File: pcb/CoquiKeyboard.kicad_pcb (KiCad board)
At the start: 2 copper layers, 307.2 x 79.8 mm, 126 parts, among them SW1 SW_Push, U1 ATmega32U4-AU, Y1 16MHz

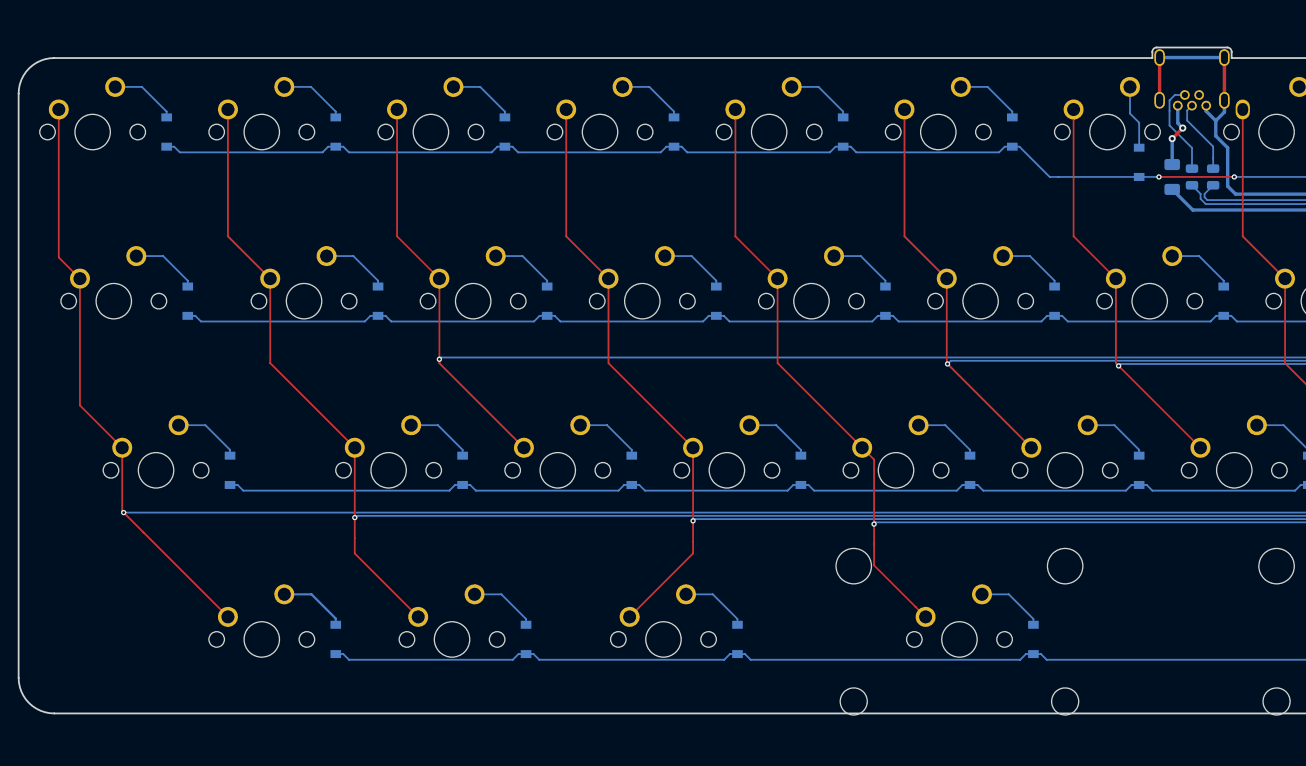
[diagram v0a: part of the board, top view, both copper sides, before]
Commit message: update schematics to use with newer USB-C
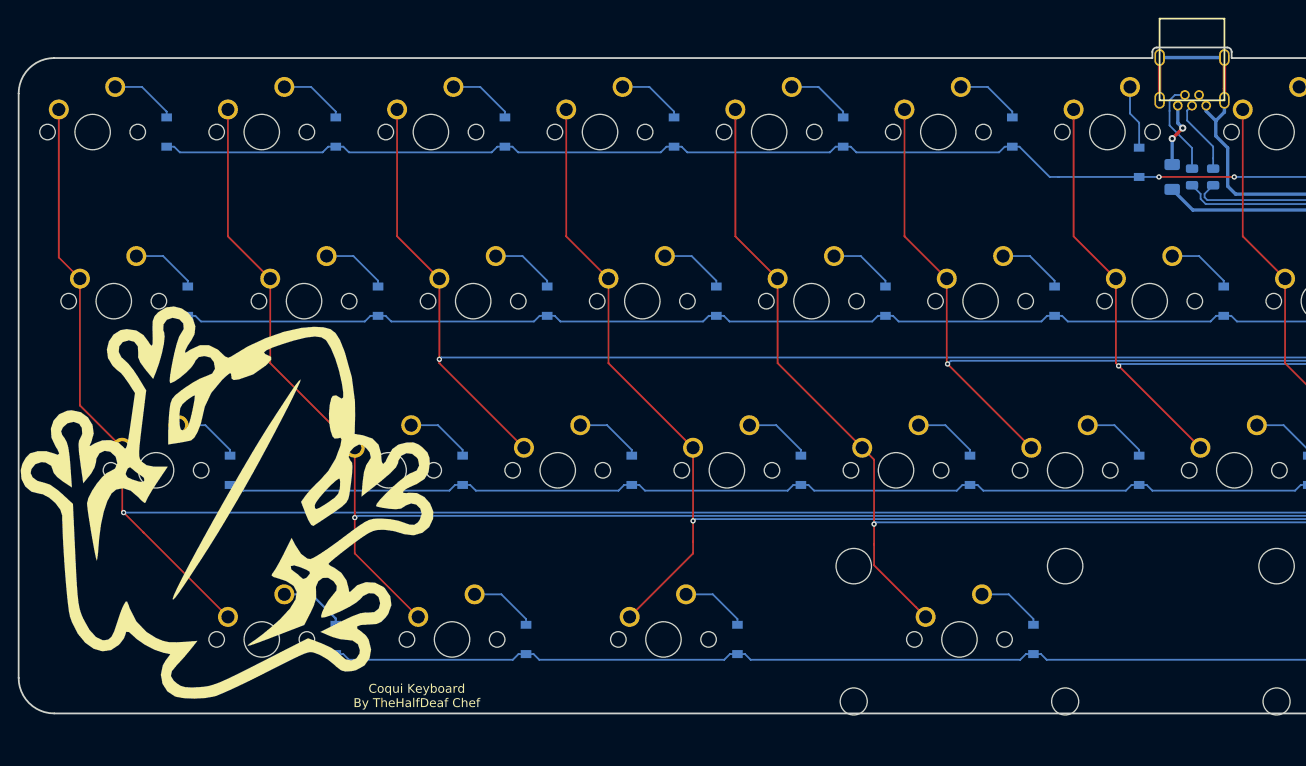
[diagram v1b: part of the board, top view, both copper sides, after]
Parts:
- added G***: LOGO, pcb:CoquiLogo, F.Cu at (44.5, 69.1)
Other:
- board text added: "Coqui Keyboard By TheHalfDeaf Chef"

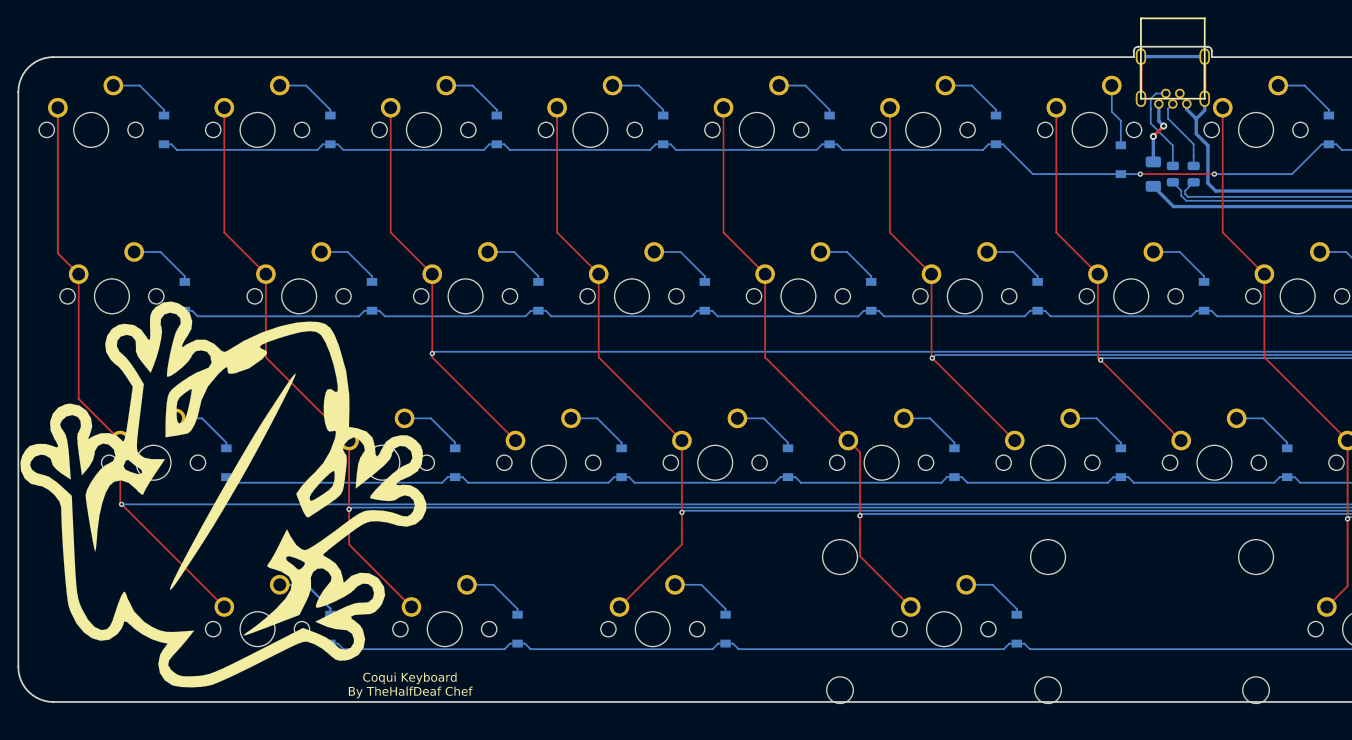
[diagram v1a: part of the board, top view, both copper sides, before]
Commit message: replaced old footprint with new
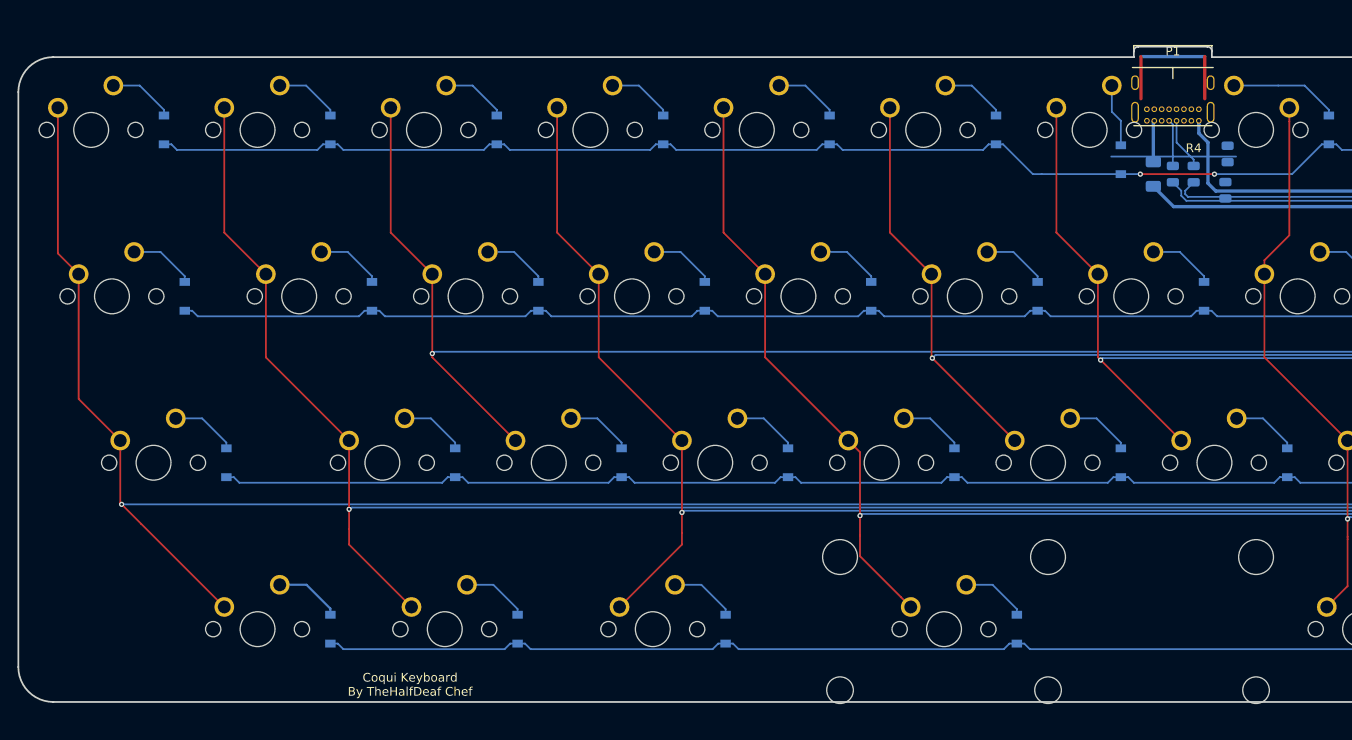
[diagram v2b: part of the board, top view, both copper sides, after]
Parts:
- removed G***: LOGO, pcb:CoquiLogo
- removed USB1: USB Mini, local:USB-Mini-B_ LCSC-C46398
- added P1: USB_C_Plug_USB2.0, Type-C:USB_C_GCT_USB4085, F.Cu at (152.4, 21.4)
- added R1: 5k1, Resistor_SMD:R_0805_2012Metric, B.Cu at (158.4, 35.5)
- added R2: 5k1, Resistor_SMD:R_0805_2012Metric, B.Cu at (158.7, 31.3)
- MX26: renamed from MX8; moved to B.Cu
- turned MX26 to 180 degrees
- renumbered D18 to D10, D32 to D11, D4 to D12, D19 to D13, D33 to D14, D46 to D15, D5 to D16, D20 to D17, D34 to D18, D47 to D19, D16 to D2, D6 to D20, D35 to D22, D7 to D23, D22 to D24, D36 to D25, D8 to D26, D23 to D27, D37 to D28, D48 to D29, D30 to D3, D9 to D30, D24 to D31, D38 to D32, D10 to D33, D25 to D34, D39 to D35, D49 to D36, D11 to D37, D26 to D38, D40 to D39, D44 to D4, D50 to D40, D12 to D41, D27 to D42, D41 to D43, D51 to D44, D13 to D45, D28 to D46, D52 to D47, D14 to D48, D42 to D49, D2 to D5, D53 to D50, D15 to D51, D29 to D52, D43 to D53, D17 to D6, D31 to D7, D45 to D8, D3 to D9, MX18 to MX10, MX32 to MX11, MX4 to MX12, MX19 to MX13, MX33 to MX14, MX46 to MX15, MX5 to MX16, MX20 to MX17, MX34 to MX18, MX47 to MX19, MX16 to MX2, MX6 to MX20, MX35 to MX22, MX7 to MX23, MX22 to MX24, MX36 to MX25, MX23 to MX27, MX37 to MX28, MX48 to MX29, MX30 to MX3, MX9 to MX30, MX24 to MX31, MX38 to MX32, MX10 to MX33, MX25 to MX34, MX39 to MX35, MX49 to MX36, MX11 to MX37, MX26 to MX38, MX40 to MX39, MX44 to MX4, MX50 to MX40, MX12 to MX41, MX27 to MX42, MX41 to MX43, MX51 to MX44, MX13 to MX45, MX28 to MX46, MX52 to MX47, MX14 to MX48, MX42 to MX49, MX2 to MX5, MX53 to MX50, MX15 to MX51, MX29 to MX52, MX43 to MX53, MX17 to MX6, MX31 to MX7, MX45 to MX8, MX3 to MX9, R2 to R4, R1 to R5, R4 to R6
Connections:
- U1 pad 1: Net-(U1-Pad1) -> (no net)
- U1 pad 10: Net-(U1-Pad10) -> (no net)
- U1 pad 11: Net-(U1-Pad11) -> (no net)
- U1 pad 12: Net-(U1-Pad12) -> (no net)
- U1 pad 36: Net-(U1-Pad36) -> (no net)
- U1 pad 42: Net-(U1-Pad42) -> (no net)
- U1 pad 9: Net-(U1-Pad9) -> (no net)
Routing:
- net Net-(P1-PadB5): track 0.00 -> 14.3 mm
- net D-: track 10.7 -> 5.34 mm
- net GND: track 288.5 -> 283.3 mm
- net Net-(D26-Pad2): track 7.60 -> 12.7 mm
- net VCC: track 7.36 -> 4.75 mm, vias 2 -> 0
- net D+: track 8.54 -> 5.98 mm
- net colH: track 217.0 -> 216.2 mm

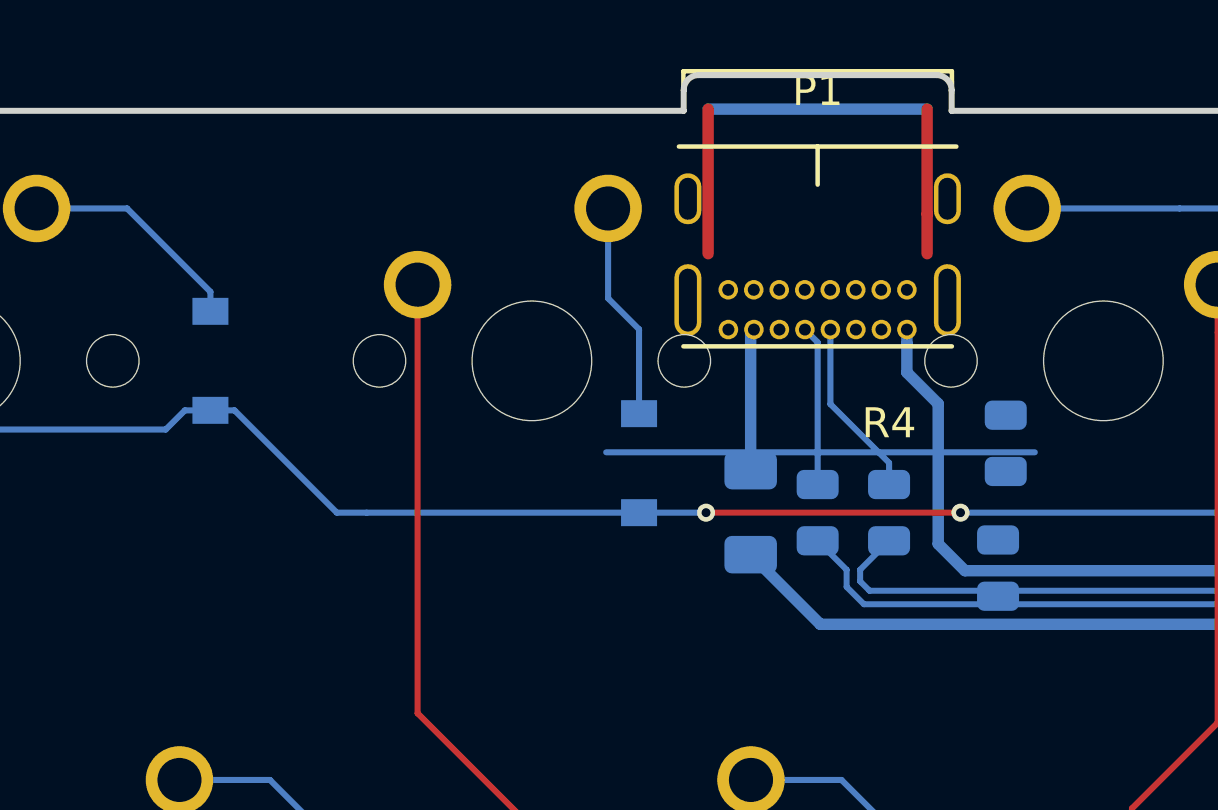
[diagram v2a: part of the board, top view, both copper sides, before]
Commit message: reconnect resistors and diodes to USB C
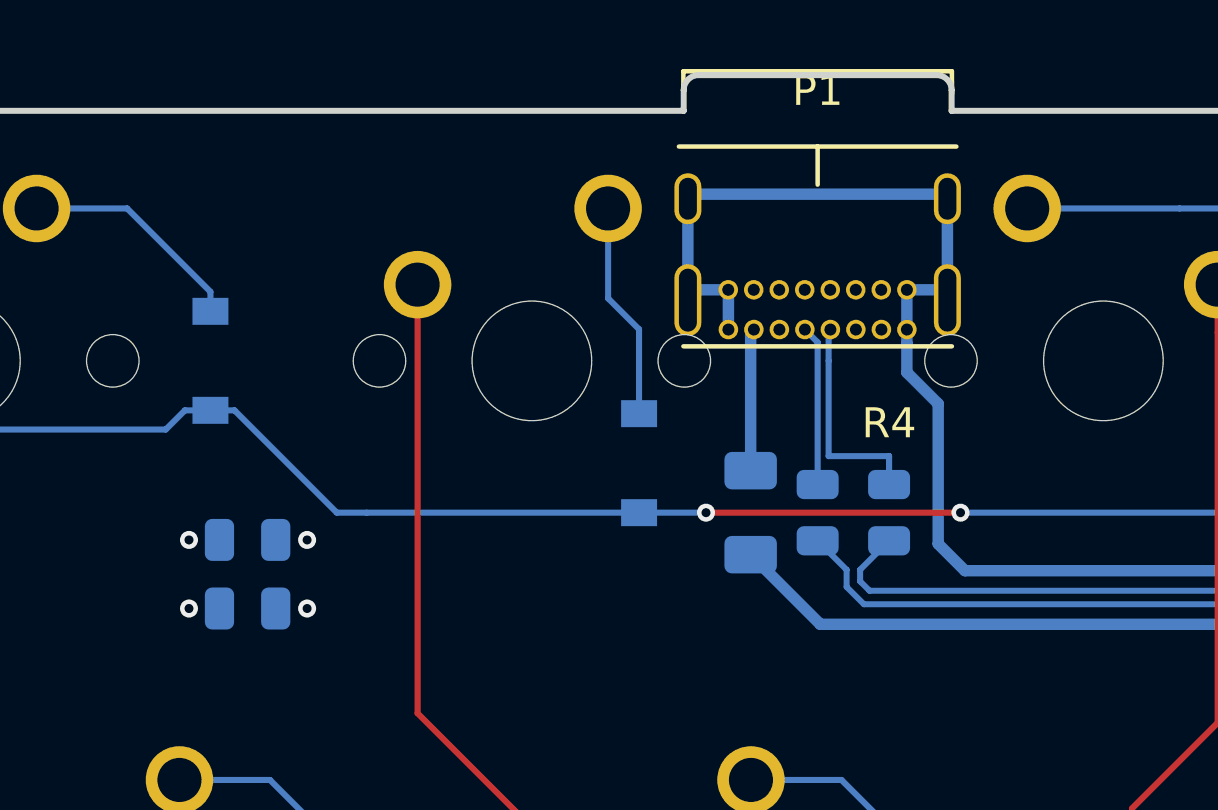
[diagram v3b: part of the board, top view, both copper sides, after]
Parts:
- moved R2 25.9 mm to (133.4, 36.8), turned to 0 degrees
- moved R1 25.0 mm to (133.4, 34.5), turned to 0 degrees
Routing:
- net Net-(P1-PadB5): track 14.3 -> 0.00 mm
- net GND: track 283.3 -> 287.5 mm
- net D+: track 5.98 -> 6.91 mm
- net (no net): vias 0 -> 4
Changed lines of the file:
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@@
     (thickness 1.6)
     (drawings 18)
-    (tracks 843)
+    (tracks 857)
     (zones 0)
     (modules 128)
@@
   )
   (module Resistor_SMD:R_0805_2012Metric (layer B.Cu)
-    (at 158.413749 35.48325 90)
+    (at 133.3985 34.544)
     (descr "Resistor SMD 0805 (2012 Metric), square (rectangular) end terminal, IPC_7351 nominal, (Body size source: https://docs.google.com/spreadsheets/d/1BsfQQcO9C6DZCsRaXUlFlo91Tg2WpOkGARC1WS5S8t0/edit?usp=sharing), generated with kicad-footprint-generator")
     (tags resistor)
     (attr smd)
-    (fp_text reference R1 (at 0 1.65 90) (layer B.SilkS)
+    (fp_text reference R1 (at 0 1.65) (layer B.SilkS)
       (effects (font (size 1 1) (thickness 0.15)) (justify mirror))
     )
-    (fp_text value 5k1 (at 0 -1.65 90) (layer B.Fab)
+    (fp_text value 5k1 (at 0 -1.65) (layer B.Fab)
       (effects (font (size 1 1) (thickness 0.15)) (justify mirror))
     )
-    (fp_text user %R (at 0 0 90) (layer B.Fab)
+    (fp_text user %R (at 0 0) (layer B.Fab)
       (effects (font (size 0.5 0.5) (thickness 0.08)) (justify mirror))
     )
@@
     (fp_line (start -1 0.6) (end 1 0.6) (layer B.Fab) (width 0.1))
     (fp_line (start -1 -0.6) (end -1 0.6) (layer B.Fab) (width 0.1))
-    (pad 2 smd roundrect (at 0.9375 0 90) (size 0.975 1.4) (layers B.Cu B.Paste B.Mask) (roundrect_rratio 0.25)
+    (pad 2 smd roundrect (at 0.9375 0) (size 0.975 1.4) (layers B.Cu B.Paste B.Mask) (roundrect_rratio 0.25)
       (net 84 "Net-(P1-PadA5)"))
-    (pad 1 smd roundrect (at -0.9375 0 90) (size 0.975 1.4) (layers B.Cu B.Paste B.Mask) (roundrect_rratio 0.25)
+    (pad 1 smd roundrect (at -0.9375 0) (size 0.975 1.4) (layers B.Cu B.Paste B.Mask) (roundrect_rratio 0.25)
       (net 1 GND))
     (model ${KISYS3DMOD}/Resistor_SMD.3dshapes/R_0805_2012Metric.wrl
@@
   )
   (module Resistor_SMD:R_0805_2012Metric (layer B.Cu)
-    (at 158.67075 31.324251 270)
+    (at 133.3985 36.83)
     (descr "Resistor SMD 0805 (2012 Metric), square (rectangular) end terminal, IPC_7351 nominal, (Body size source: https://docs.google.com/spreadsheets/d/1BsfQQcO9C6DZCsRaXUlFlo91Tg2WpOkGARC1WS5S8t0/edit?usp=sharing), generated with kicad-footprint-generator")
     (tags resistor)
     (attr smd)
-    (fp_text reference R2 (at 0 1.65 90) (layer B.SilkS)
+    (fp_text reference R2 (at 0 1.65) (layer B.SilkS)
       (effects (font (size 1 1) (thickness 0.15)) (justify mirror))
     )
-    (fp_text value 5k1 (at 0 -1.65 90) (layer B.Fab)
+    (fp_text value 5k1 (at 0 -1.65) (layer B.Fab)
       (effects (font (size 1 1) (thickness 0.15)) (justify mirror))
     )
@@
     (fp_line (start 1.68 0.95) (end 1.68 -0.95) (layer B.CrtYd) (width 0.05))
     (fp_line (start 1.68 -0.95) (end -1.68 -0.95) (layer B.CrtYd) (width 0.05))
-    (fp_text user %R (at 0 0 180) (layer B.Fab)
+    (fp_text user %R (at 0 0 270) (layer B.Fab)
       (effects (font (size 0.5 0.5) (thickness 0.08)) (justify mirror))
     )
-    (pad 1 smd roundrect (at -0.9375 0 270) (size 0.975 1.4) (layers B.Cu B.Paste B.Mask) (roundrect_rratio 0.25)
+    (pad 1 smd roundrect (at -0.9375 0) (size 0.975 1.4) (layers B.Cu B.Paste B.Mask) (roundrect_rratio 0.25)
       (net 1 GND))
-    (pad 2 smd roundrect (at 0.9375 0 270) (size 0.975 1.4) (layers B.Cu B.Paste B.Mask) (roundrect_rratio 0.25)
+    (pad 2 smd roundrect (at 0.9375 0) (size 0.975 1.4) (layers B.Cu B.Paste B.Mask) (roundrect_rratio 0.25)
       (net 85 "Net-(P1-PadB5)"))
     (model ${KISYS3DMOD}/Resistor_SMD.3dshapes/R_0805_2012Metric.wrl
@@
   (gr_line (start 327.421616 24.240624) (end 327.421616 94.821808) (layer Edge.Cuts) (width 0.2))
   (gr_line (start 156.864728 20.240624) (end 323.421616 20.240624) (layer Edge.Cuts) (width 0.2))
-  (segment (start 148.75 25.00312) (end 148.75 20.18312) (width 0.381) (layer F.Cu) (net 1))
-  (segment (start 156.05 23.67212) (end 156.05 20.18312) (width 0.381) (layer F.Cu) (net 1))
-  (segment (start 148.75 20.18312) (end 156.05 20.18312) (width 0.381) (layer B.Cu) (net 1))
+  (via (at 135.382 36.83) (size 0.6) (drill 0.3) (layers F.Cu B.Cu) (net 0))
+  (via (at 131.445 36.83) (size 0.6) (drill 0.3) (layers F.Cu B.Cu) (net 0))
+  (via (at 131.445 34.544) (size 0.6) (drill 0.3) (layers F.Cu B.Cu) (net 0))
+  (via (at 135.382 34.544) (size 0.6) (drill 0.3) (layers F.Cu B.Cu) (net 0))
   (segment (start 305.290912 54.247624) (end 304.159912 54.247624) (width 0.381) (layer B.Cu) (net 1))
   (segment (start 309.059912 52.878624) (end 307.690912 54.247624) (width 0.381) (layer B.Cu) (net 1))
@@
   (segment (start 323.894276 53.578096) (end 323.894276 52.778096) (width 0.381) (layer B.Cu) (net 1))
   (segment (start 319.578264 51.79216) (end 322.361464 51.79216) (width 0.381) (layer B.Cu) (net 1))
-  (segment (start 156.05 25.00312) (end 156.05 23.67212) (width 0.381) (layer F.Cu) (net 1))
   (segment (start 155.375 27.990869) (end 155.375 27.53125) (width 0.381) (layer B.Cu) (net 1))
   (segment (start 155.375 28.963142) (end 155.375 27.990869) (width 0.381) (layer B.Cu) (net 1))
@@
   (segment (start 156.418244 34.67694) (end 156.418244 30.006386) (width 0.381) (layer B.Cu) (net 1))
   (segment (start 307.627492 35.569908) (end 157.311212 35.569908) (width 0.381) (layer B.Cu) (net 1))
+  (segment (start 148.2275 23.01875) (end 148.075 23.17125) (width 0.381) (layer B.Cu) (net 1))
+  (segment (start 156.725 23.17125) (end 156.5725 23.01875) (width 0.381) (layer B.Cu) (net 1))
+  (segment (start 156.5725 23.01875) (end 148.2275 23.01875) (width 0.381) (layer B.Cu) (net 1))
+  (segment (start 149.425 26.21125) (end 149.42 26.20625) (width 0.381) (layer B.Cu) (net 1))
+  (segment (start 149.425 27.53125) (end 149.425 26.21125) (width 0.381) (layer B.Cu) (net 1))
+  (segment (start 155.375 27.53125) (end 155.375 26.20625) (width 0.381) (layer B.Cu) (net 1))
+  (segment (start 156.725 26.55125) (end 156.725 23.17125) (width 0.381) (layer B.Cu) (net 1))
+  (segment (start 156.38 26.20625) (end 156.725 26.55125) (width 0.381) (layer B.Cu) (net 1))
+  (segment (start 155.375 26.20625) (end 156.38 26.20625) (width 0.381) (layer B.Cu) (net 1))
+  (segment (start 148.42 26.20625) (end 148.075 26.55125) (width 0.381) (layer B.Cu) (net 1))
+  (segment (start 149.42 26.20625) (end 148.42 26.20625) (width 0.381) (layer B.Cu) (net 1))
+  (segment (start 148.075 26.55125) (end 148.075 23.17125) (width 0.381) (layer B.Cu) (net 1))
   (segment (start 315.559912 55.047624) (end 317.61772 55.047624) (width 0.381) (layer B.Cu) (net 2))
   (segment (start 317.61772 55.047624) (end 318.640764 54.02458) (width 0.381) (layer B.Cu) (net 2))
@@
   (segment (start 152.399888 27.956138) (end 151.975 27.53125) (width 0.2032) (layer B.Cu) (net 51))
   (segment (start 152.399888 32.697644) (end 152.399888 27.956138) (width 0.2032) (layer B.Cu) (net 51))
-  (segment (start 154.781364 32.697644) (end 154.781364 31.972364) (width 0.2032) (layer B.Cu) (net 52))
-  (segment (start 152.825 30.016) (end 152.825 27.53125) (width 0.2032) (layer B.Cu) (net 52))
-  (segment (start 154.781364 31.972364) (end 152.825 30.016) (width 0.2032) (layer B.Cu) (net 52))
+  (segment (start 154.781364 32.697644) (end 154.781364 31.750114) (width 0.2032) (layer B.Cu) (net 52))
+  (segment (start 154.781364 31.750114) (end 154.78125 31.75) (width 0.2032) (layer B.Cu) (net 52))
+  (segment (start 154.78125 31.75) (end 152.765658 31.75) (width 0.2032) (layer B.Cu) (net 52))
+  (segment (start 152.765658 31.75) (end 152.765658 28.575) (width 0.2032) (layer B.Cu) (net 52))
+  (segment (start 152.765658 28.575) (end 152.765658 27.804632) (width 0.2032) (layer B.Cu) (net 52))
   (segment (start 127.396875 64.3718) (end 127.396875 65.025) (width 0.2032) (layer B.Cu) (net 53))
   (segment (start 124.620075 61.595) (end 127.396875 64.3718) (width 0.2032) (layer B.Cu) (net 53))
@@
   (segment (start 318.16908 59.903592) (end 318.16908 63.386256) (width 0.2032) (layer B.Cu) (net 83))
   (via (at 310.157948 83.939008) (size 0.6) (drill 0.3) (layers F.Cu B.Cu) (net 83))
-  (segment (start 159.639 31.623) (end 145.3515 31.623) (width 0.2032) (layer B.Cu) (net 85))
+  (segment (start 134.501398 34.544) (end 134.336 34.544) (width 0.25) (layer B.Cu) (net 84))
   (segment (start 315.559912 54.247624) (end 317.227096 54.247624) (width 0.25) (layer B.Cu) (net 86))
   (segment (start 317.227096 54.247624) (end 317.598968 53.875752) (width 0.25) (layer B.Cu) (net 86))
